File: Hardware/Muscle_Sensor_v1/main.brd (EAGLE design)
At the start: 76 x 42 mm, 35 parts, among them IC1 TL084D, IC2 TL7660D, IC3 LM358D, U1 AD8221AR

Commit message: Update Muscle_Sensor_v1
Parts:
- removed IC3: LM358D, linear:SO08
- removed LED1, LED2: (no value), led:CHIP-LED0805
- removed R11, R12: 330R, rcl:R1206
- removed R14: (no value), pot:SM-42/43B
- removed SJ2, SJ3: (no value), jumper:SJ
- removed SV3: (no value), con-lstb:MA03-1
- added H1, H2: MOUNT-HOLE3.0, holes:3,0
- added K1, K2: 61000418221, Wurth_Elektronik_Electromechanic_Board_to_Board_Connectors_rev15c:61000418221
- added R10: (no value), rcl:RTRIM3314J
- SV2: device con-lstb:MA03-1 -> con-lstb:MA04-1
- moved SV1 37.0 mm to (44.7, 38.3), turned to 0 degrees
- moved R1 29.5 mm to (45.0, 25.5), turned to 0 degrees
- moved R7 27.3 mm to (13.0, 5.00), turned to 90 degrees
- moved R9 26.5 mm to (23.0, 5.00), turned to 270 degrees
- moved R8 23.0 mm to (18.0, 5.00), turned to 270 degrees
- moved C7 21.8 mm to (33.0, 24.0), flipped to the bottom, turned to 180 degrees
- moved U1 20.9 mm to (46.0, 19.0), turned to 180 degrees
- moved D1 17.2 mm to (40.0, 32.0)
- moved C6 16.1 mm to (48.0, 12.0), turned to 270 degrees
- moved C8 15.2 mm to (44.0, 11.0), turned to 270 degrees
- moved IC1 14.4 mm to (32.0, 18.0)
- moved C4 13.7 mm to (9.00, 28.0)
- moved R2 13.5 mm to (40.0, 14.0), turned to 90 degrees
- moved C1 13.0 mm to (29.0, 10.0), turned to 180 degrees
- moved SJ1 12.3 mm to (16.0, 30.0)
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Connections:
- removed net N$12: IC3.3, SJ2.1
- removed net N$15: IC3.5, SJ3.1
- removed net N$16: IC3.6, IC3.7, R12.1
- removed net N$17: IC3.1, IC3.2, R11.1
- removed net N$18: LED1.A, R11.2
- removed net N$20: LED2.A, R12.2
- net GND: now also K1.2, K1.3, K2.2, K2.3, SV2.1; no longer IC3.4, LED1.C, LED2.C, SV2.2, SV3.1
- net N$11: now also R10.1; no longer R14.3
- net RECT: now also SV2.3; no longer SJ2.2, SV3.3
- net SIG: now also R10.2, R10.3, SV2.2; no longer R14.1, R14.2, SJ3.2, SV3.2
- net V+: now also K1.4, K2.4, SV2.4; no longer IC3.8, SV2.3
- net V-: now also K1.1, K2.1; no longer SV2.1
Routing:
- net V-: track 114.8 -> 60.6 mm, vias 3 -> 1
- net V+: track 142.5 -> 104.4 mm, vias 4 -> 3
- net N$12: track 30.1 -> 0.00 mm, vias 2 -> 0
- net N$1: track 50.8 -> 24.1 mm, vias 2 -> 0
- net N$16: track 20.2 -> 0.00 mm
- net N$15: track 16.9 -> 0.00 mm
- net MID: track 7.27 -> 23.2 mm
- net N$11: track 12.2 -> 25.9 mm
- net SIG: track 79.0 -> 66.3 mm, vias 3 -> 1
- net N$20: track 12.3 -> 0.00 mm
- net N$17: track 11.9 -> 0.00 mm
- net RECT: track 73.5 -> 62.5 mm, vias 0 -> 2
- net N$18: track 7.94 -> 0.00 mm
- net N$7: track 20.8 -> 26.5 mm
- net N$6: track 20.9 -> 15.5 mm
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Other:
- board size 76 x 42 mm -> 50 x 40 mm

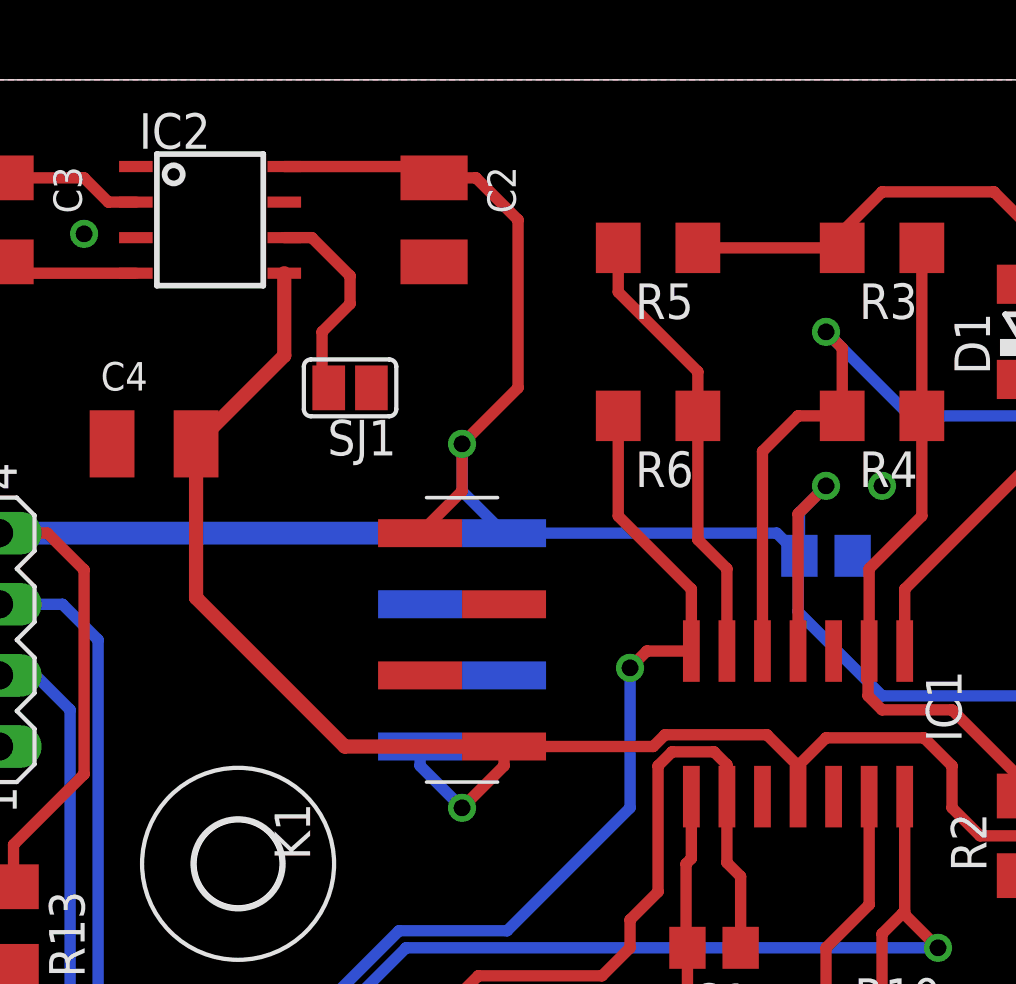
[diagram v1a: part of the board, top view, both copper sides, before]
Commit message: Muscle Sensor Updates
Schematic and board updates fixes some bugs of first version.
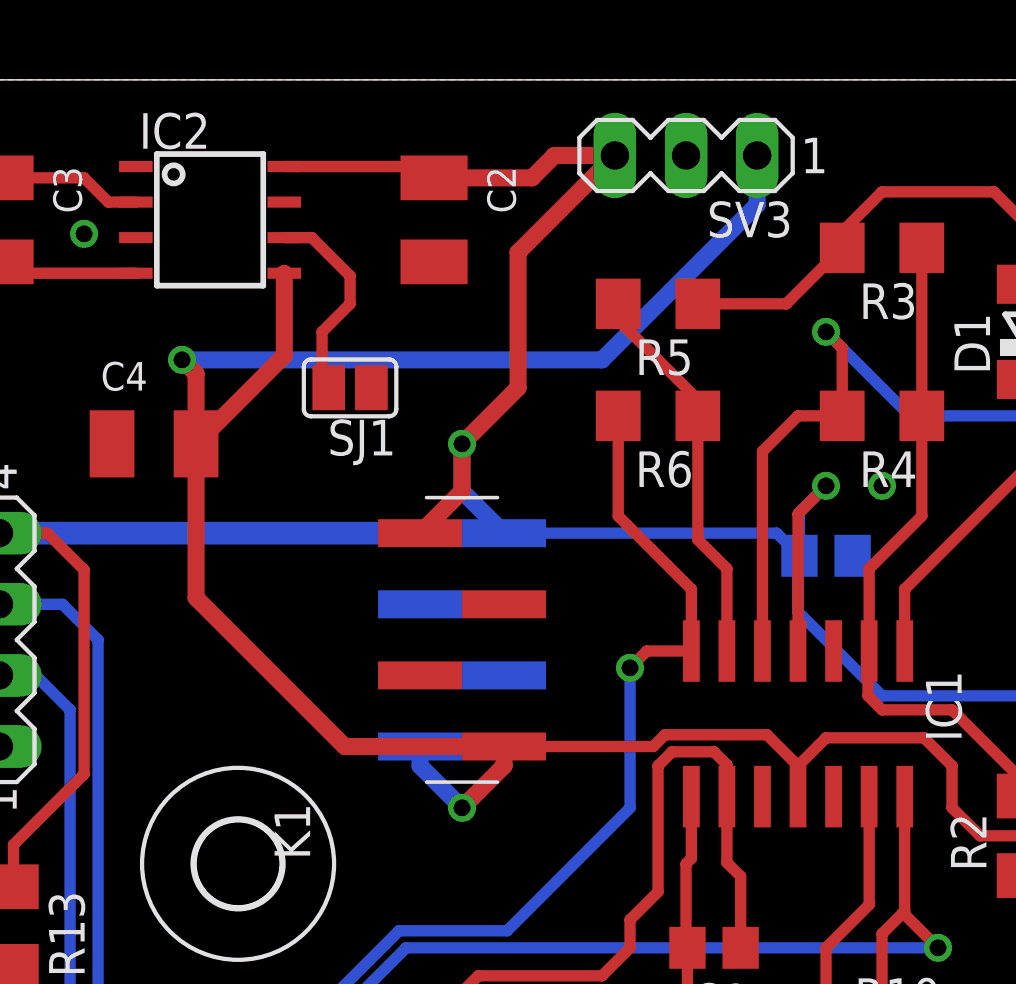
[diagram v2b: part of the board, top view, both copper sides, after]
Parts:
- added SV3: (no value), con-lstb:MA03-1
- moved R5 2.00 mm to (27.0, 33.0)
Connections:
- net GND: now also SV3.2
- net V+: now also SV3.3
- net V-: now also SV3.1
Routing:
- net V-: track 60.6 -> 88.4 mm, vias 1 -> 2
- net V+: track 104.4 -> 111.3 mm
- net N$8: track 16.0 -> 14.0 mm
- net N$6: track 15.5 -> 16.3 mm
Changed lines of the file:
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@@
 <dimension x1="0" y1="-2" x2="50" y2="-2" x3="25" y3="-3" textsize="1.778" layer="48"/>
 <dimension x1="53" y1="1" x2="53" y2="41" x3="54" y3="21" textsize="1.778" layer="48" dtype="vertical"/>
+<dimension x1="-6" y1="13" x2="-6" y2="1" x3="-5" y3="7" textsize="1.778" layer="48"/>
 </plain>
 <attributes>
@@
 <attribute name="VALUE" x="36.27" y="31.54" size="1.27" layer="27" rot="R180"/>
 </element>
-<element name="R5" library="rcl" library_urn="urn:adsk.eagle:library:334" package="R1206" package3d_urn="urn:adsk.eagle:package:23540/2" value="150k" x="27" y="35" smashed="yes" rot="R180">
-<attribute name="NAME" x="28.27" y="33.73" size="1.27" layer="25" rot="R180"/>
-<attribute name="SPICEPREFIX" value="R" x="-2.21" y="71.83" size="1.778" layer="27" rot="R180" display="off"/>
-<attribute name="VALUE" x="28.27" y="37.54" size="1.27" layer="27" rot="R180"/>
+<element name="R5" library="rcl" library_urn="urn:adsk.eagle:library:334" package="R1206" package3d_urn="urn:adsk.eagle:package:23540/2" value="150k" x="27" y="33" smashed="yes" rot="R180">
+<attribute name="NAME" x="28.27" y="31.73" size="1.27" layer="25" rot="R180"/>
+<attribute name="SPICEPREFIX" value="R" x="-2.21" y="69.83" size="1.778" layer="27" rot="R180" display="off"/>
+<attribute name="VALUE" x="28.27" y="35.54" size="1.27" layer="27" rot="R180"/>
 </element>
 <element name="R6" library="rcl" library_urn="urn:adsk.eagle:library:334" package="R1206" package3d_urn="urn:adsk.eagle:package:23540/2" value="150k" x="27" y="29" smashed="yes" rot="R180">
@@
 <element name="H1" library="holes" library_urn="urn:adsk.eagle:library:237" package="3,0" package3d_urn="urn:adsk.eagle:package:14277/1" value="MOUNT-HOLE3.0" x="46" y="5" smashed="yes"/>
 <element name="H2" library="holes" library_urn="urn:adsk.eagle:library:237" package="3,0" package3d_urn="urn:adsk.eagle:package:14277/1" value="MOUNT-HOLE3.0" x="12" y="13" smashed="yes"/>
+<element name="SV3" library="con-lstb" library_urn="urn:adsk.eagle:library:162" package="MA03-1" package3d_urn="urn:adsk.eagle:package:8339/1" value="" x="28" y="38.3" smashed="yes" rot="R180">
+<attribute name="MF" value="" x="28" y="38.3" size="1.778" layer="27" rot="R180" display="off"/>
+<attribute name="MPN" value="" x="28" y="38.3" size="1.778" layer="27" rot="R180" display="off"/>
+<attribute name="NAME" x="31.81" y="36.649" size="1.27" layer="25" ratio="10" rot="R180"/>
+<attribute name="OC_FARNELL" value="unknown" x="28" y="38.3" size="1.778" layer="27" rot="R180" display="off"/>
+<attribute name="OC_NEWARK" value="unknown" x="28" y="38.3" size="1.778" layer="27" rot="R180" display="off"/>
+<attribute name="VALUE" x="31.81" y="41.221" size="1.27" layer="27" ratio="10" rot="R180"/>
+</element>
 </elements>
 <signals>
@@
 <via x="42" y="17" extent="1-16" drill="0.6" shape="octagon"/>
 <via x="46" y="11" extent="1-16" drill="0.6" shape="octagon"/>
+<contactref element="SV3" pad="2"/>
 </signal>
 <signal name="MID">
@@
 <contactref element="K1" pad="1"/>
 <contactref element="K2" pad="1"/>
-<wire x1="13.65" y1="34.095" x2="13.65" y2="31.15" width="0.508" layer="1"/>
-<wire x1="13.65" y1="31.15" x2="10.5" y2="28" width="0.508" layer="1"/>
-<wire x1="10.5" y1="28" x2="10.5" y2="22.5" width="0.508" layer="1"/>
-<wire x1="15.81" y1="17.19" x2="21.5" y2="17.19" width="0.508" layer="1"/>
-<wire x1="10.5" y1="22.5" x2="15.81" y2="17.19" width="0.508" layer="1"/>
 <via x="20" y="15" extent="1-16" drill="0.6" shape="octagon"/>
 <wire x1="44.095" y1="16.4" x2="44.095" y2="15.095" width="0.4064" layer="1"/>
@@
 <wire x1="37.5" y1="15" x2="37.5" y2="16.5" width="0.4064" layer="1"/>
 <wire x1="38.5" y1="14" x2="37.5" y2="15" width="0.4064" layer="1"/>
-<wire x1="21.5" y1="17.19" x2="21.5" y2="16.5" width="0.4064" layer="1"/>
-<wire x1="21.5" y1="16.5" x2="20" y2="15" width="0.4064" layer="1"/>
-<wire x1="18.5" y1="17.19" x2="18.5" y2="16.5" width="0.4064" layer="16"/>
-<wire x1="18.5" y1="16.5" x2="20" y2="15" width="0.4064" layer="16"/>
+<contactref element="SV3" pad="1"/>
+<wire x1="30.54" y1="38.3" x2="30.54" y2="36.54" width="0.6096" layer="16"/>
+<via x="10" y="31" extent="1-16" drill="0.6" shape="octagon"/>
+<wire x1="30.54" y1="36.54" x2="25" y2="31" width="0.6096" layer="16"/>
+<wire x1="25" y1="31" x2="10" y2="31" width="0.6096" layer="16"/>
+<wire x1="21.5" y1="17.19" x2="21.5" y2="16.5" width="0.6096" layer="1"/>
+<wire x1="21.5" y1="16.5" x2="20" y2="15" width="0.6096" layer="1"/>
+<wire x1="21.5" y1="17.19" x2="15.81" y2="17.19" width="0.6096" layer="1"/>
+<wire x1="10.5" y1="22.5" x2="10.5" y2="28" width="0.6096" layer="1"/>
+<wire x1="15.81" y1="17.19" x2="10.5" y2="22.5" width="0.6096" layer="1"/>
+<wire x1="20" y1="15" x2="18.5" y2="16.5" width="0.6096" layer="16"/>
+<wire x1="18.5" y1="16.5" x2="18.5" y2="17.19" width="0.6096" layer="16"/>
+<wire x1="13.65" y1="34.095" x2="13.65" y2="31.15" width="0.6096" layer="1"/>
+<wire x1="13.65" y1="31.15" x2="10.5" y2="28" width="0.6096" layer="1"/>
+<wire x1="10.5" y1="28" x2="10.5" y2="30.5" width="0.6096" layer="1"/>
+<wire x1="10.5" y1="30.5" x2="10" y2="31" width="0.6096" layer="1"/>
 </signal>
 <signal name="V+">
@@
 <wire x1="21.5" y1="24.81" x2="31.24" y2="24.81" width="0.4064" layer="16"/>
 <wire x1="31.24" y1="24.81" x2="32.05" y2="24" width="0.4064" layer="16"/>
-<wire x1="19" y1="37.5" x2="20.5" y2="37.5" width="0.4064" layer="1"/>
-<wire x1="20.5" y1="37.5" x2="22" y2="36" width="0.4064" layer="1"/>
-<wire x1="22" y1="36" x2="22" y2="30" width="0.4064" layer="1"/>
-<wire x1="22" y1="30" x2="20" y2="28" width="0.4064" layer="1"/>
 <via x="20" y="28" extent="1-16" drill="0.6" shape="octagon"/>
-<wire x1="20" y1="28" x2="20" y2="26.31" width="0.4064" layer="16"/>
-<wire x1="20" y1="26.31" x2="21.5" y2="24.81" width="0.4064" layer="16"/>
-<wire x1="20" y1="28" x2="20" y2="26.31" width="0.4064" layer="1"/>
-<wire x1="20" y1="26.31" x2="18.5" y2="24.81" width="0.4064" layer="1"/>
 <wire x1="32" y1="20.6" x2="32" y2="25.5" width="0.4064" layer="1"/>
 <wire x1="32" y1="25.5" x2="33" y2="26.5" width="0.4064" layer="1"/>
@@
 <wire x1="6.5" y1="16.202" x2="3.98" y2="13.682" width="0.4064" layer="1"/>
 <wire x1="3.98" y1="13.682" x2="3.98" y2="12.182" width="0.4064" layer="1"/>
+<contactref element="SV3" pad="3"/>
+<wire x1="18.5" y1="24.81" x2="20" y2="26.31" width="0.6096" layer="1"/>
+<wire x1="20" y1="26.31" x2="20" y2="28" width="0.6096" layer="1"/>
+<wire x1="21.5" y1="24.81" x2="20" y2="26.31" width="0.6096" layer="16"/>
+<wire x1="20" y1="26.31" x2="20" y2="28" width="0.6096" layer="16"/>
+<wire x1="20" y1="28" x2="22" y2="30" width="0.6096" layer="1"/>
+<wire x1="22" y1="34.84" x2="25.46" y2="38.3" width="0.6096" layer="1"/>
+<wire x1="22" y1="30" x2="22" y2="34.84" width="0.6096" layer="1"/>
+<wire x1="25.46" y1="38.3" x2="23.3" y2="38.3" width="0.6096" layer="1"/>
+<wire x1="22.5" y1="37.5" x2="19" y2="37.5" width="0.6096" layer="1"/>
+<wire x1="23.3" y1="38.3" x2="22.5" y2="37.5" width="0.6096" layer="1"/>
 </signal>
 <signal name="RECT">
@@
 <contactref element="D1" pad="A"/>
 <contactref element="R5" pad="1"/>
-<wire x1="28.422" y1="35" x2="33.578" y2="35" width="0.4064" layer="1"/>
+<wire x1="31.578" y1="33" x2="33.578" y2="35" width="0.4064" layer="1"/>
+<wire x1="31.578" y1="33" x2="28.422" y2="33" width="0.4064" layer="1"/>
 <wire x1="40" y1="33.7" x2="40" y2="36" width="0.4064" layer="1"/>
 <wire x1="40" y1="36" x2="39" y2="37" width="0.4064" layer="1"/>
@@
 <wire x1="28.422" y1="24.578" x2="28.422" y2="29" width="0.4064" layer="1"/>
 <wire x1="29.46" y1="23.54" x2="28.422" y2="24.578" width="0.4064" layer="1"/>
-<wire x1="28.422" y1="29" x2="28.422" y2="30.578" width="0.4064" layer="1"/>
-<wire x1="25.578" y1="33.422" x2="25.578" y2="35" width="0.4064" layer="1"/>
-<wire x1="28.422" y1="30.578" x2="25.578" y2="33.422" width="0.4064" layer="1"/>
+<wire x1="28.422" y1="29" x2="28.422" y2="29.578" width="0.4064" layer="1"/>
+<wire x1="25.578" y1="32.422" x2="25.578" y2="33" width="0.4064" layer="1"/>
+<wire x1="28.422" y1="29.578" x2="25.578" y2="32.422" width="0.4064" layer="1"/>
 </signal>
 <signal name="N$9">
